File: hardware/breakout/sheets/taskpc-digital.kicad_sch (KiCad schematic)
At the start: 75 parts, among them J2 Connector 0 (analog + AISENSE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, J3 Connector 1 (digital, task PC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, J4 Manual reward button (panel, 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, J5 Remote reward BNC (parallel t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, J6 Reward driver out (BNC), U10 SN74AHCT541PW, U11 SN74AHCT541PW, U12 SN74HCT32D, U13 SN74HCT14D, U5 SN74LVC541APW, U6 SN74LVC541APW, U69 74HCT123D, U7 SN74LVC541APW, U70 SN74AHCT541PW, U71 SN74AHCT541PW, U72 SN74AHCT541PW, U73 SN74AHCT541PW, U8 SN74AHCT541PW, U9 SN74AHCT541PW

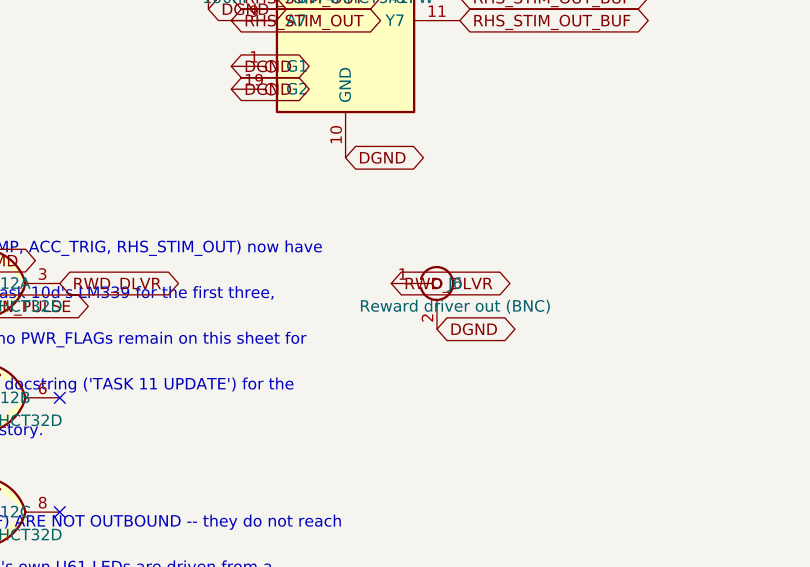
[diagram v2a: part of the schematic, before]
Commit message: fix(hardware): one driver and one series resistor per panel output (F4, M3)
F4 -- FOUR CAMERA TRIGGERS SHARED ONE UNTERMINATED OUTPUT.

CAM_TRIG_BEH drove J14-J17 from a single SN74AHCT541 output. Four parallel
coax runs present Z0/4 ~ 12.5 ohm, so the initial edge drew roughly 118 mA
against the part's 25 mA per-output ABSOLUTE maximum -- brief, but on every
edge for the life of the board. With no source termination the cameras
could also see reflections and double-trigger, which is corrupted frame
timing rather than a cosmetic fault.

Each of the five triggers now has its own buffer channel and its own 47 ohm
series resistor: CAM_TRIG_BEH splits into CAM_TRIG_BEH1..4, channel 2 of the
existing trigger buffer keeps trigger 1, and a new package (U74) takes the
other three. They still share one trigger RATE via CAM_TRIG_BEH_RAW -- spec
Sec.9.4 is unchanged -- they no longer share a driver pin.

NOT on finding F1's spare channels, which the audit expected. Those sit on
taskpc-digital, and routing an unbuffered 3.3 V trigger across the board and
its buffered copies back again is the wrong trade for a signal whose entire
problem is edge quality at the connector. Source GPIO, buffer and BNCs stay
on one sheet; the cost is one package.

47 ohm errs high on purpose. An AHCT541's own output impedance is ~25-35
ohm, so textbook series termination into 50 ohm coax would be nearer 20 ohm.
Over-damping costs a little edge rate and buys margin against the failure
that actually matters here. The first step at a high-impedance camera input
lands at ~77% of the swing before settling, far above any TTL V_IH.

M3 -- SIX BARE PANEL OUTPUTS, AND THERE WERE ELEVEN.

Series resistance added to all six the finding names: the five camera
triggers at 47 ohm, and J6 (reward driver out) at 100 ohm -- that pin's
problem is fault current from an inductive kick or a mis-plug, not
transmission-line matching, so it takes this board's established
panel-series value rather than the termination one. 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
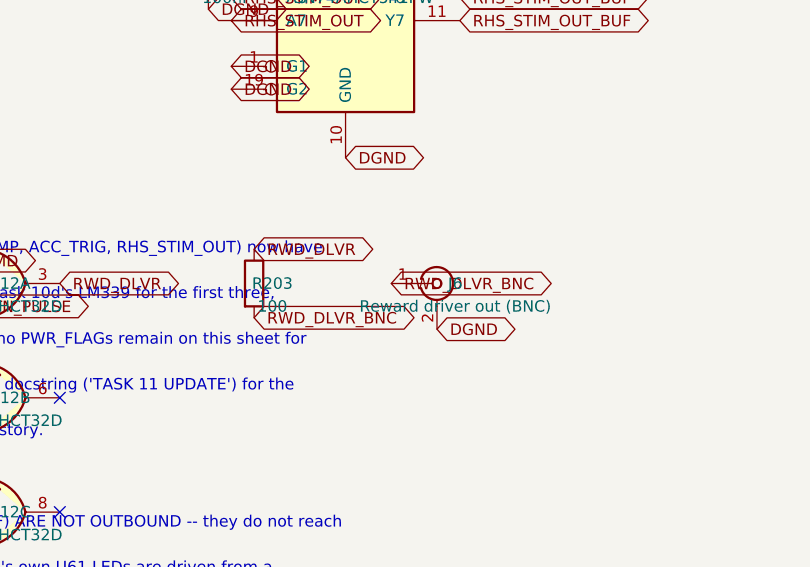
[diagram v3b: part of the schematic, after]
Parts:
- added R203: 100, Resistor_SMD:R_0603_1608Metric, symbol Device:R
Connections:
- net RWD_DLVR: now also R203.1; no longer J6.1 (In)
- new net RWD_DLVR_BNC: J6.1 (In), R203.2
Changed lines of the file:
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@@
 		)
 	)
-	(global_label "RWD_DLVR"
+	(global_label "RWD_DLVR_BNC"
 		(shape bidirectional)
 		(at 224.79 294.64 0)
@@
 			(effects (font (size 1.27 1.27)) (hide yes))
 		)
+	)
+	(symbol
+		(lib_id "Device:R")
+		(at 209.55 294.64 0)
+		(unit 1)
+		(exclude_from_sim no)
+		(in_bom yes)
+		(on_board yes)
+		(dnp no)
+		(property "Reference" "R203"
+			(at 211.58200000000002 294.64 0)
+			(effects (font (size 1.27 1.27)))
+		)
+		(property "Value" "100"
+			(at 211.58200000000002 297.18 0)
+			(effects (font (size 1.27 1.27)))
+		)
+		(property "Footprint" "Resistor_SMD:R_0603_1608Metric"
+			(at 209.55 294.64 0)
+			(effects (font (size 1.27 1.27)) (hide yes))
+		)
+		(property "Datasheet" ""
+			(at 209.55 294.64 0)
+			(effects (font (size 1.27 1.27)) (hide yes))
+		)
+		(pin "1")
+		(pin "2")
+		(instances
+			(project "breakout"
+				(path "/d2c4d978-5db4-46d9-a1cd-a7af0aeb1700/caf42f3d-f02c-45ed-97e6-3311ce1b5ca0"
+					(reference "R203") (unit 1)
+				)
+			)
+		)
+	)
+	(global_label "RWD_DLVR"
+		(shape bidirectional)
+		(at 209.55 290.83 0)
+		(effects (font (size 1.27 1.27)) (justify left))
+		(property "Intersheetrefs" "${INTERSHEET_REFS}"
+			(at 209.55 290.83 0)
+			(effects (font (size 1.27 1.27)) (hide yes))
+		)
+	)
+	(global_label "RWD_DLVR_BNC"
+		(shape bidirectional)
+		(at 209.55 298.45 0)
+		(effects (font (size 1.27 1.27)) (justify left))
+		(property "Intersheetrefs" "${INTERSHEET_REFS}"
+			(at 209.55 298.45 0)
+			(effects (font (size 1.27 1.27)) (hide yes))
+		)

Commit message: fix(hardware): rebuild the connectors on their primary drawings (F6, R1, D3)
Audit step 5, the mechanical half. Three connectors changed, one of them a
fab-stopper, and none of it was visible to the netlist.

MDR68 (the fab-stopper). Rebuilt from MH drawing 3700-0121-01 rev 3.0. The
as-built footprint drilled contacts at 0.5 mm against a required 0.85 mm -- the
pins do not fit, so the board could not have been assembled -- and laid them out
as 2 rows at 2.84 mm where the drawing shows 4 staggered rows of 17 at 1.905 mm.
The 4-row stagger is what makes an 0.85 mm drill manufacturable at a 1.27 mm
mating pitch at all; the array now spans the drawing's own 41.91 mm exactly,
which is the arithmetic that confirms the reading. The claim made during the
audit that it had "no mounting holes at all" was wrong: it had two, Ø2.79 on
57.9 mm centres against the drawing's Ø2.77 on 57.93.

M12 (ruling R1). M12A_5_Panel is deleted, symbol and footprint and generator
function alike. Its contact geometry was sourced well -- IEC 61076-2-101
A-coding, cross-checked three ways -- and it made no difference, because the part
the design procures (Phoenix 1551833) terminates in AWG 22-20 wire and mounts
through the panel. It has no PCB tails, so no board-mount footprint of any
dimensions could have been right, and as built every cable insertion and every
3-4 N.m tightening loaded PCB pads directly. J1 is now a stock 5-way header where
those flying leads land; the connector stays in the order BOM as chassis
furniture.

BNC (F6). BNC_PanelMountable_Vertical puts the connector axis perpendicular to
the PCB -- a 9.65 mm barrel hole through the board -- so on a 430x240 mm board
lying flat in a 2U chassis all 31 barrels pointed at the lid rather than at the
panels. It also cost 5,654 mm2 of pad and 2,267 mm2 of removed copper on every
layer. Replaced by a right-angle dual jack built from Amphenol drawing 31-6575
rev A: 31 ports on 17 bodies, 3 spare ports, every shell still routed
individually.
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
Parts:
- removed J5: Remote reward BNC (parallel to panel button; lock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, Connector_Coaxial:BNC_PanelMountable_Vertical, symbol Connector:Conn_Coaxial
- removed J6: Reward driver out (BNC), Connector_Coaxial:BNC_PanelMountable_Vertical, symbol Connector:Conn_Coaxial
- added J5: Dual panel BNC: Remote reward BNC (parallel to pa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, wl-sync:BNC_Dual_RA_Isolated, symbol wl-sync:BNC_Dual_RA_Isolated
- added J6: Dual panel BNC: Reward driver out (BNC) | Spare p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, wl-sync:BNC_Dual_RA_Isolated, symbol wl-sync:BNC_Dual_RA_Isolated
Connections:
- net DGND: now also J5.2 (A_Ext), J5.4 (B_Ext), J6.2 (A_Ext), J6.4 (B_Ext)
- net RWD_BTN: now also J5.1 (A_In)
- net RWD_DLVR_BNC: now also J6.1 (A_In)
- no-connect marks 113 -> 115
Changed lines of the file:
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@@
 	)
 	(symbol
-		(lib_id "Connector:Conn_Coaxial")
+		(lib_id "wl-sync:BNC_Dual_RA_Isolated")
 		(at 20.32 314.96 0)
 		(unit 1)
@@
 			(effects (font (size 1.27 1.27)))
 		)
-		(property "Value" "Remote reward BNC (parallel to panel button; locking -- no TRS mating transient)"
+		(property "Value" "Dual panel BNC: Remote reward BNC (parallel to panel button; locking -- no TRS mating transient) | Spare panel BNC (2nd port of the reward remote's dual body, FRONT face)"
 			(at 22.352 317.5 0)
 			(effects (font (size 1.27 1.27)))
 		)
-		(property "Footprint" "Connector_Coaxial:BNC_PanelMountable_Vertical"
+		(property "Footprint" "wl-sync:BNC_Dual_RA_Isolated"
 			(at 20.32 314.96 0)
 			(effects (font (size 1.27 1.27)) (hide yes))
@@
 		(property "Intersheetrefs" "${INTERSHEET_REFS}"
 			(at 20.32 320.03999999999996 0)
+			(effects (font (size 1.27 1.27)) (hide yes))
+		)
+	)
+	(symbol
+		(lib_id "wl-sync:BNC_Dual_RA_Isolated")
+		(at 20.32 325.12 0)
+		(unit 2)
+		(exclude_from_sim no)
+		(in_bom yes)
+		(on_board yes)
+		(dnp no)
+		(property "Reference" "J5"
+			(at 22.352 325.12 0)
+			(effects (font (size 1.27 1.27)))
+		)
+		(property "Value" "Dual panel BNC: Remote reward BNC (parallel to panel button; locking -- no TRS mating transient) | Spare panel BNC (2nd port of the reward remote's dual body, FRONT face)"
+			(at 22.352 327.66 0)
+			(effects (font (size 1.27 1.27)))
+		)
+		(property "Footprint" "wl-sync:BNC_Dual_RA_Isolated"
+			(at 20.32 325.12 0)
+			(effects (font (size 1.27 1.27)) (hide yes))
+		)
+		(property "Datasheet" ""
+			(at 20.32 325.12 0)
+			(effects (font (size 1.27 1.27)) (hide yes))
+		)
+		(pin "3")
+		(pin "4")
+		(instances
+			(project "breakout"
+				(path "/d2c4d978-5db4-46d9-a1cd-a7af0aeb1700/caf42f3d-f02c-45ed-97e6-3311ce1b5ca0"
+					(reference "J5") (unit 2)
+				)
+			)
+		)
+	)
+	(no_connect
+		(at 15.24 325.12)
+	)
+	(global_label "DGND"
+		(shape bidirectional)
+		(at 20.32 330.2 0)
+		(effects (font (size 1.27 1.27)) (justify left))
+		(property "Intersheetrefs" "${INTERSHEET_REFS}"
+			(at 20.32 330.2 0)
 			(effects (font (size 1.27 1.27)) (hide yes))
 		)
@@
 	)
 	(symbol
-		(lib_id "Connector:Conn_Coaxial")
+		(lib_id "wl-sync:BNC_Dual_RA_Isolated")
 		(at 229.87 294.64 0)
 		(unit 1)
@@
 			(effects (font (size 1.27 1.27)))
 		)
-		(property "Value" "Reward driver out (BNC)"
+		(property "Value" "Dual panel BNC: Reward driver out (BNC) | Spare panel BNC (2nd port of the reward driver-out dual body, BACK face)"
 			(at 231.90200000000002 297.18 0)
 			(effects (font (size 1.27 1.27)))
 		)
-		(property "Footprint" "Connector_Coaxial:BNC_PanelMountable_Vertical"
+		(property "Footprint" "wl-sync:BNC_Dual_RA_Isolated"
 			(at 229.87 294.64 0)
 			(effects (font (size 1.27 1.27)) (hide yes))
@@
 			(effects (font (size 1.27 1.27)) (hide yes))
 		)
+	)
+	(symbol
+		(lib_id "wl-sync:BNC_Dual_RA_Isolated")
+		(at 229.87 304.8 0)
+		(unit 2)
+		(exclude_from_sim no)
+		(in_bom yes)
+		(on_board yes)
+		(dnp no)
+		(property "Reference" "J6"
+			(at 231.90200000000002 304.8 0)
+			(effects (font (size 1.27 1.27)))
+		)
+		(property "Value" "Dual panel BNC: Reward driver out (BNC) | Spare panel BNC (2nd port of the reward driver-out dual body, BACK face)"
+			(at 231.90200000000002 307.34000000000003 0)
+			(effects (font (size 1.27 1.27)))
+		)
+		(property "Footprint" "wl-sync:BNC_Dual_RA_Isolated"
+			(at 229.87 304.8 0)
+			(effects (font (size 1.27 1.27)) (hide yes))
+		)
+		(property "Datasheet" ""
+			(at 229.87 304.8 0)
+			(effects (font (size 1.27 1.27)) (hide yes))
+		)
+		(pin "3")
+		(pin "4")
+		(instances
+			(project "breakout"
+				(path "/d2c4d978-5db4-46d9-a1cd-a7af0aeb1700/caf42f3d-f02c-45ed-97e6-3311ce1b5ca0"
+					(reference "J6") (unit 2)
+				)
+			)
+		)
+	)
+	(no_connect
+		(at 224.79 304.8)
+	)
+	(global_label "DGND"
+		(shape bidirectional)
+		(at 229.87 309.88 0)
+		(effects (font (size 1.27 1.27)) (justify left))
+		(property "Intersheetrefs" "${INTERSHEET_REFS}"
+			(at 229.87 309.88 0)
+			(effects (font (size 1.27 1.27)) (hide yes))
+		)

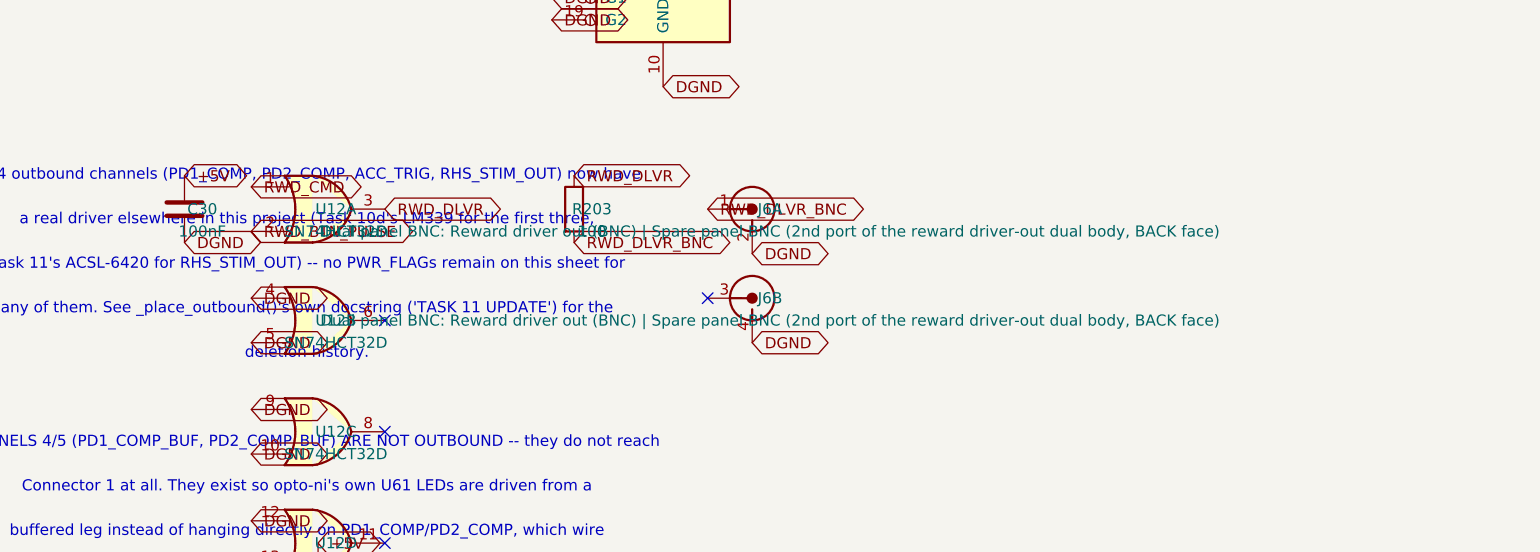
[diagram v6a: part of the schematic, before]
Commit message: feat(hardware): frame-time inputs -- camera strobes back to GPIO26/27
Closes the gap camera-sync-change.md §3 opened. With the cameras free-running,
spec §12 item 1's justification for dropping exposure-active returns ("the Pi
triggers the cameras so frame times are known by construction") is false in
both halves. One FLIR ExposureActive strobe per camera group now returns on a
spare back-panel BNC and is timestamped in the same event stream as everything
else.

WHY A COMPARATOR AND NOT THIS BOARD'S USUAL INBOUND BUFFER. The strobe's best
published low is 0.87 V against SN74LVC541A's 0.8 V V_IL max -- a SILENT 70 mV
miss, on a signal that looks perfectly correct on a scope. A comparator is also
the only option here whose margin is a design choice rather than a datasheet
coincidence, which matters because FLIR label the whole table "values are for
reference only".

WHY +12V AND NOT +5V. The LM339's input common-mode ceiling is V+ - 1.5V to
V+ - 2.0V. The strobe's HIGH is 5.0 V (pulled up to +5V through 1k, FLIR's own
published row -- a stiffer pull-up makes V_low worse, not better). On a +5V
supply that ceiling is 3.0-3.5 V and the input sits above it, which is the
LM339's best-known failure mode. +12V/AGND matches U54 exactly.

GROUND DOMAINS, WHICH THE FIRST PASS GOT BACKWARDS. The pull-up sources from
+5V, whose return is DGND, so the shell net decides where 4.2 mA of switching
current flows: on AGND it would cross NT1, the single star tie, on every camera
frame; on DGND it never does. Shells, clamps and the threshold divider are
therefore DGND. V- stays AGND and does not enter the comparison -- both inputs
are DGND-referenced, so the offset is common-mode and cancels -- it sets only
the output LOW level, exactly as it already does for PD1_COMP/PD2_COMP/ACC_TRIG.

Tying the spare sections' inputs to DGND made U76 a SECOND AGND/DGND bridge
alongside NT1; check_breakout_power_netlist.py caught it. They go to AGND, this
part's own V-. A negative control now reproduce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
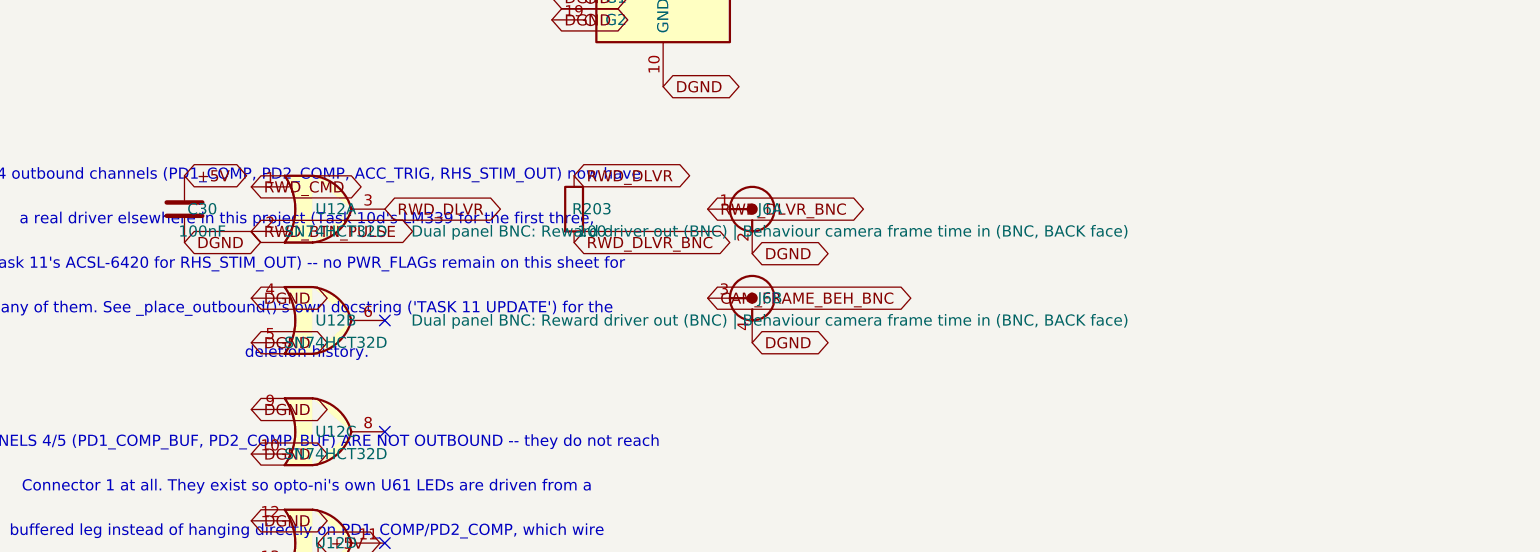
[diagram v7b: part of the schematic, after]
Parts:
- J6: value Dual panel BNC: Reward driver out (BNC) | Spare panel BNC (2nd port of the reward driver-out dual body, BACK face) -> Dual panel BNC: Reward driver out (BNC) | Behaviour camera frame time in (BNC, BACK face)
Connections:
- net CAM_FRAME_BEH_BNC: now reaches J6.3 (B_In)
- no-connect marks 115 -> 114
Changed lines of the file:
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@@
 			(effects (font (size 1.27 1.27)))
 		)
-		(property "Value" "Dual panel BNC: Reward driver out (BNC) | Spare panel BNC (2nd port of the reward driver-out dual body, BACK face)"
+		(property "Value" "Dual panel BNC: Reward driver out (BNC) | Behaviour camera frame time in (BNC, BACK face)"
 			(at 231.90200000000002 297.18 0)
 			(effects (font (size 1.27 1.27)))
@@
 			(effects (font (size 1.27 1.27)))
 		)
-		(property "Value" "Dual panel BNC: Reward driver out (BNC) | Spare panel BNC (2nd port of the reward driver-out dual body, BACK face)"
+		(property "Value" "Dual panel BNC: Reward driver out (BNC) | Behaviour camera frame time in (BNC, BACK face)"
 			(at 231.90200000000002 307.34000000000003 0)
 			(effects (font (size 1.27 1.27)))
@@
 		)
 	)
-	(no_connect
-		(at 224.79 304.8)
+	(global_label "CAM_FRAME_BEH_BNC"
+		(shape bidirectional)
+		(at 224.79 304.8 0)
+		(effects (font (size 1.27 1.27)) (justify left))
+		(property "Intersheetrefs" "${INTERSHEET_REFS}"
+			(at 224.79 304.8 0)
+			(effects (font (size 1.27 1.27)) (hide yes))
+		)
 	)
 	(global_label "DGND"
